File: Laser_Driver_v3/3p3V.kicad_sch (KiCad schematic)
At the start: 16 parts, among them U4 MC7812CTG, U5 MC7805CTG, U6 LT3045EMSE 3.3V, U7 LP5907MFX-1.8

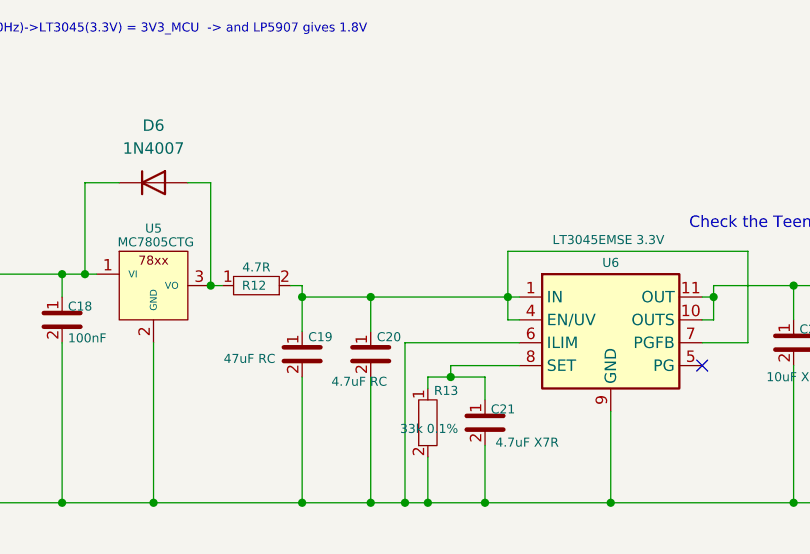
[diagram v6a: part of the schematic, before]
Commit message: Adding rail voltage good led circuitry.
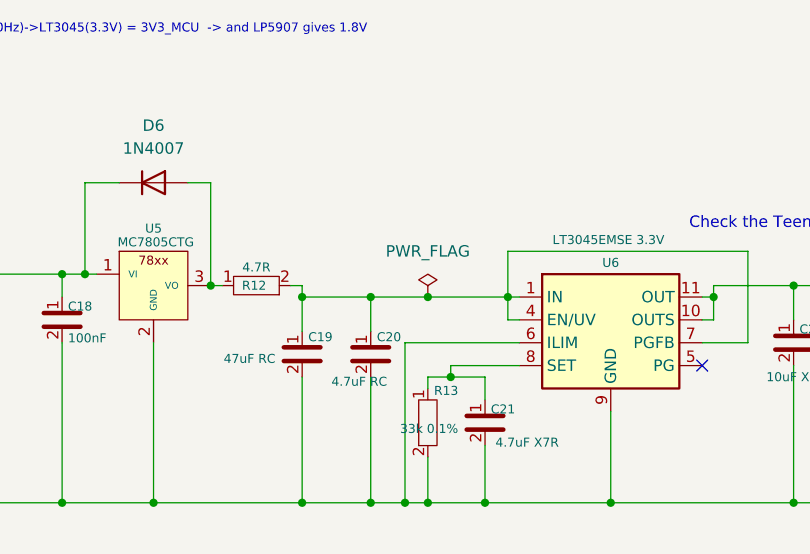
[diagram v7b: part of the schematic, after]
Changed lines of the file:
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@@
+	)
+	(junction
+		(at 147.32 58.42)
+		(diameter 0)
+		(color 0 0 0 0)
 	)
 	(junction
@@
 	(wire
 		(pts
-			(xy 133.35 58.42) (xy 156.21 58.42)
+			(xy 133.35 58.42) (xy 147.32 58.42)
 		)
 		(stroke
@@
 		(pts
 			(xy 153.67 69.85) (xy 153.67 67.31)
+		)
+		(stroke
+			(width 0)
+			(type default)
+		)
+	)
+	(wire
+		(pts
+			(xy 147.32 58.42) (xy 156.21 58.42)
 		)
 		(stroke
@@
 					(unit 1)
 				)
+			)
+		)
+	)
+	(symbol
+		(lib_id "power:PWR_FLAG")
+		(at 147.32 58.42 0)
+		(unit 1)
+		(body_style 1)
+		(exclude_from_sim no)
+		(in_bom yes)
+		(on_board yes)
+		(in_pos_files yes)
+		(dnp no)
+		(fields_autoplaced yes)
+		(property "Reference" "#FLG03"
+			(at 147.32 56.515 0)
+			(hide yes)
+			(show_name no)
+			(do_not_autoplace no)
+			(effects
+				(font
+					(size 1.27 1.27)
+				)
+			)
+		)
+		(property "Value" "PWR_FLAG"
+			(at 147.32 53.34 0)
+			(show_name no)
+			(do_not_autoplace no)
+			(effects
+				(font
+					(size 1.27 1.27)
+				)
+			)
+		)
+		(property "Footprint" ""
+			(at 147.32 58.42 0)
+			(hide yes)
+			(show_name no)
+			(do_not_autoplace no)
+			(effects
+				(font
+					(size 1.27 1.27)
+				)
+			)
+		)
+		(property "Datasheet" ""
+			(at 147.32 58.42 0)
+			(hide yes)
+			(show_name no)
+			(do_not_autoplace no)
+			(effects
+				(font
+					(size 1.27 1.27)
+				)
+			)
+		)
+		(property "Description" "Special symbol for telling ERC where power comes from"
+			(at 147.32 58.42 0)
+			(hide yes)
+			(show_name no)
+			(do_not_autoplace no)
+			(effects
+				(font
+					(size 1.27 1.27)
+				)
+			)
+		)
+		(pin "1"
+		)
+		(instances
+			(project "laser_driver_v3_Power"
+				(path "/b2c3d4e5-f6a7-8901-bcde-f12345678901/8f1d8420-6d65-4b14-9d89-baaedfa51091"
+					(reference "#FLG03")
+					(unit 1)
+				)
